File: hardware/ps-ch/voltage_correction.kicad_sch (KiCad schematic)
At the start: 35 parts, among them Q10 MMBT3904, Q5 MMBT3906, Q6 MMBT3906, Q7 MMBT3904, Q8 MMBT3904, U7 OPA992IDCKR, U8 OPA992IDCKR

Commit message: did some wiring
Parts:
- removed R37: R, symbol Device:R
- added C39, C42, C43, C75: C, symbol Device:C
- added L12: L, symbol Device:L
- added R29, R30, R31, R32, R33, R34: R, symbol Device:R
- added U9: OPA992IDCKR, symbol ps-ch:OPA992IDCKR
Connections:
- net GND: now also C42.2, C43.2, C75.2, R32.2, R33.1, U9.2 (V-)
- net VDC: now also C75.1, L12.1
- net VSENSE_SCALED renamed VSENSE
- net VSENSE: now also C39.1, R29.1, U9.4
- new net: R31.2, R32.1, U9.1 (+)
- new net: C39.2, R29.2, R30.2, U9.3 (-)
- new net: C42.1, C43.1, L12.2, U9.5 (V+)
- new net VREF+: R34.2
- new net VSENSE+: R31.1, R34.1
- new net VSENSE-: R30.1, R33.2
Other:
- note added: "VOLTAGE CORRECTION"
- moved on the sheet: C32, C35, C37, C38, C40, C44, C45, C69, C70, L10, L11, Q10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

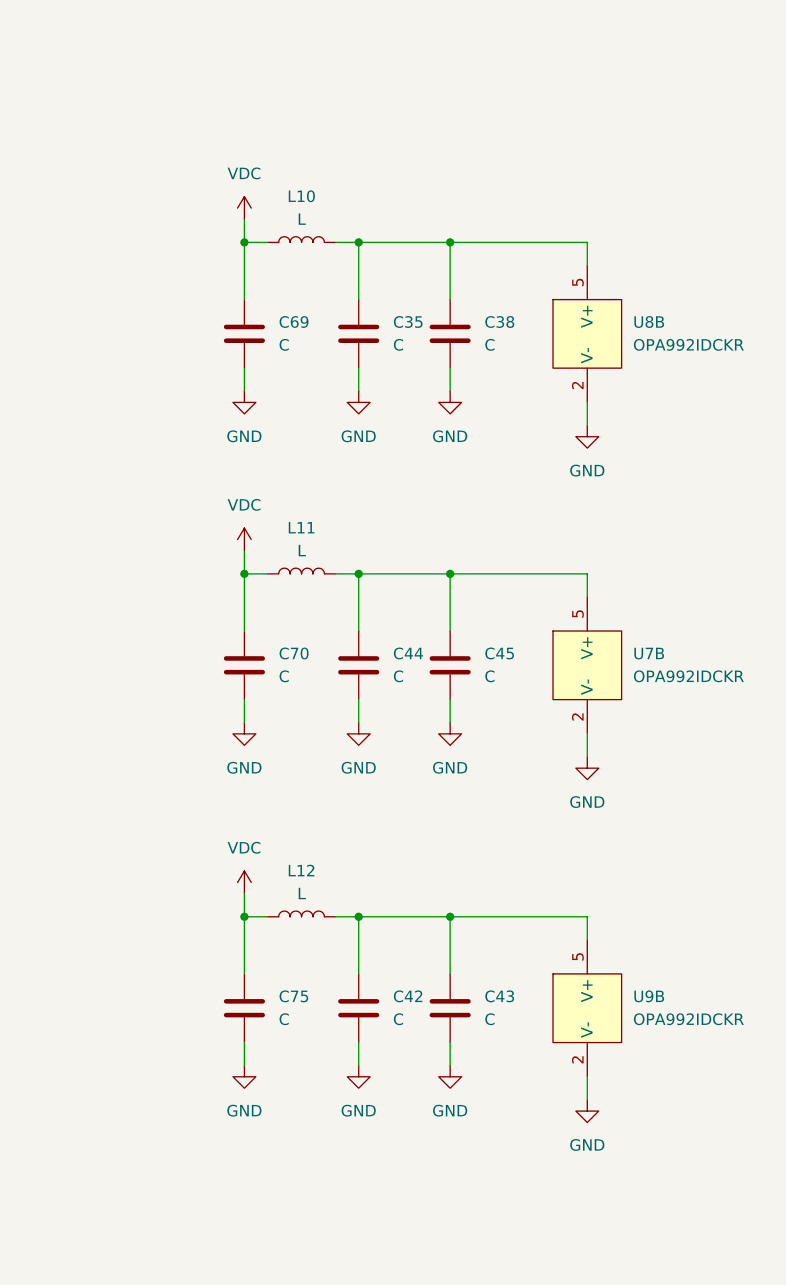
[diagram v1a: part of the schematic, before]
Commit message: added calculations and component values
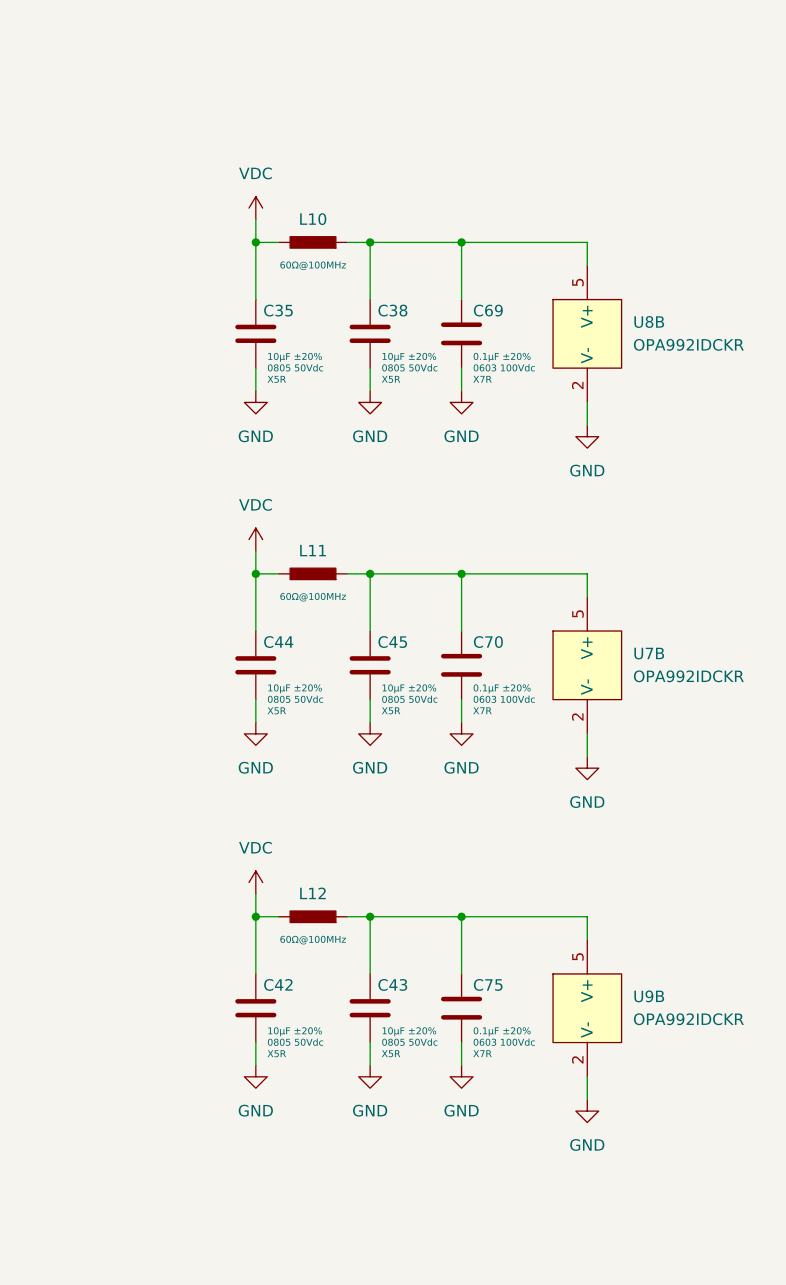
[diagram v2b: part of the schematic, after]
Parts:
- removed C35, C38, C42, C43, C44, C45, C69, C70, C75: C, symbol Device:C
- removed L10, L11, L12: L, symbol Device:L
- added C35, C38, C42, C43, C44, C45: 10μF 0805 50Vdc X5R ±20%, Capacitor_SMD:C_0805_2012Metric, symbol ps-ch:10μF 0805 50Vdc X5R ±20%
- added C69, C70, C75: 0.1μF 0603 100Vdc X7R ±20%, Capacitor_SMD:C_0603_1608Metric, symbol ps-ch:0.1μF 0603 100Vdc X7R ±20%
- added L10, L11, L12: 60Ω@100MHz, Inductor_SMD:L_0603_1608Metric, symbol ps-ch:74437349015
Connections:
- net GND: now also C35.1, C38.1, C42.1, C43.1, C44.1, C45.1, C69.1, C70.1, C75.1
- net VDC: now also C35.2, C42.2, C44.2, L10.2, L11.2, L12.2
- net at U8.5 (V+): now also C38.2, C69.2, L10.1
- net at U9.5 (V+): now also C43.2, C75.2, L12.1
- net at U7.5 (V+): now also C45.2, C70.2, L11.1

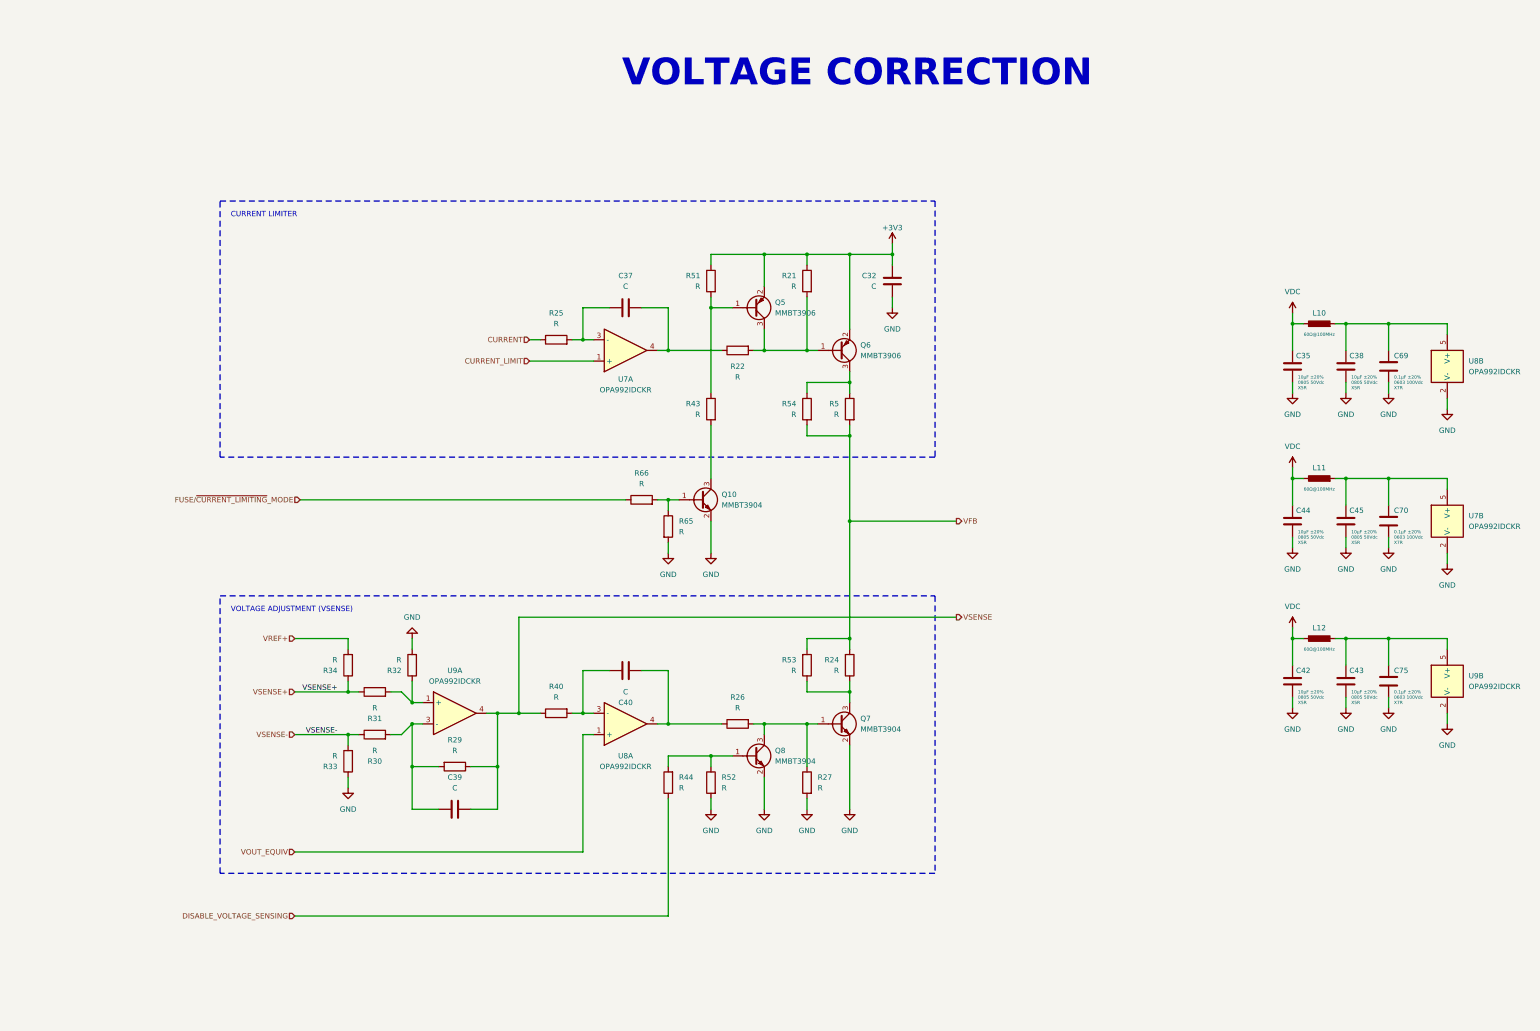
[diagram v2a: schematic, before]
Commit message: calculated voltage correction
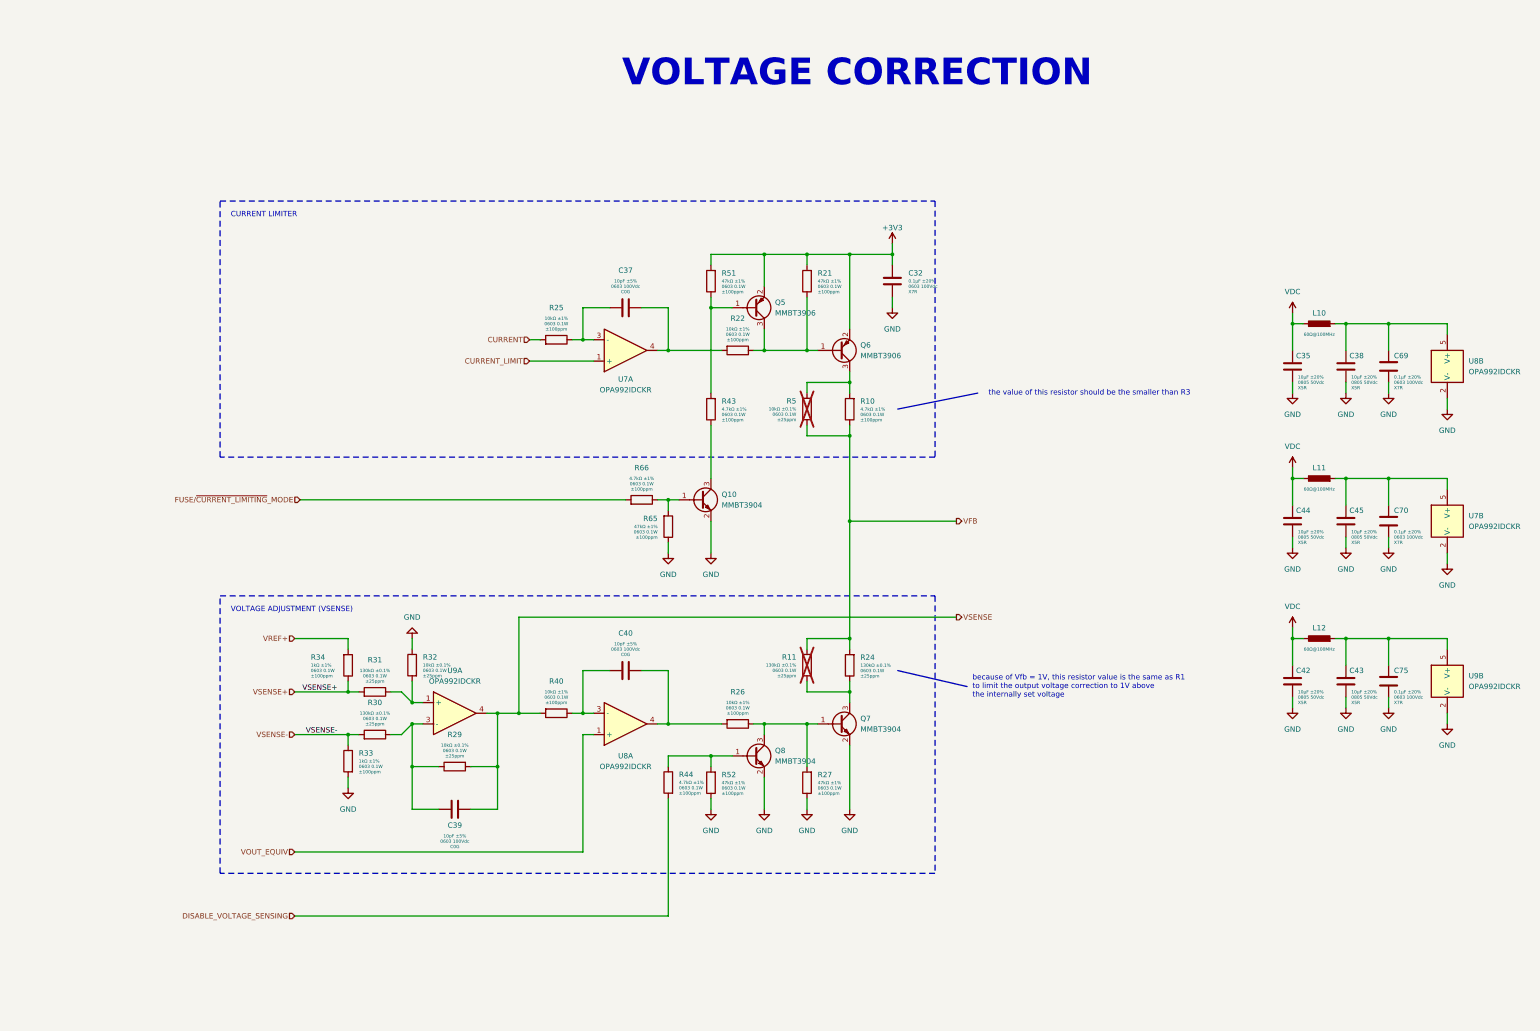
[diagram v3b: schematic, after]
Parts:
- removed R5, R53, R54: R, symbol Device:R
- added R10: 4.7kΩ 0603 0.1W ±1% ±100ppm/°C, Resistor_SMD:R_0603_1608Metric, symbol ps-ch:4.7kΩ 0603 0.1W ±1% ±100ppm/°C
- added R11: 130kΩ 0603 0.1W ±0.1% ±25ppm/°C, Resistor_SMD:R_0603_1608Metric, symbol ps-ch:130kΩ 0603 0.1W ±0.1% ±25ppm/°C
- added R5: 10kΩ 0603 0.1W ±0.1% ±25ppm/°C, Resistor_SMD:R_0603_1608Metric, symbol ps-ch:10kΩ 0603 0.1W ±0.1% ±25ppm/°C
- C32: value C -> 0.1μF 0603 100Vdc X7R ±20%; footprint (none) -> Capacitor_SMD:C_0603_1608Metric; symbol Device:C -> ps-ch:0.1μF 0603 100Vdc X7R ±20%; DisplayValue0 (none) -> 0.1μF ±20%; DisplayValue1 (none) -> 0603 100Vdc; DisplayValue2 (none) -> X7R; Manufacturer (none) -> Murata; Manufacturer Part Number (none) -> GRM188R72A104MA35
- C37, C39, C40: value C -> 10pF 0603 100Vdc C0G ±5%; footprint (none) -> Capacitor_SMD:C_0603_1608Metric; symbol Device:C -> ps-ch:10pF 0603 100Vdc C0G ±5%; DisplayValue0 (none) -> 10pF ±5%; DisplayValue1 (none) -> 0603 100Vdc; DisplayValue2 (none) -> C0G; Manufacturer (none) -> Murata; Manufacturer Part Number (none) -> GCM1885C2A100JA16
- R21, R27, R51, R52, R65: value R -> 47kΩ 0603 0.1W ±1% ±100ppm/°C; footprint (none) -> Resistor_SMD:R_0603_1608Metric; symbol Device:R -> ps-ch:47kΩ 0603 0.1W ±1% ±100ppm/°C; DisplayValue0 (none) -> 47kΩ ±1%; DisplayValue1 (none) -> 0603 0.1W; DisplayValue2 (none) -> ±100ppm; Manufacturer (none) -> Yageo; Manufacturer Part Number (none) -> AC0603FR-0747L
- R22, R25, R26, R40: value R -> 10kΩ 0603 0.1W ±1% ±100ppm/°C; footprint (none) -> Resistor_SMD:R_0603_1608Metric; symbol Device:R -> ps-ch:10kΩ 0603 0.1W ±1% ±100ppm/°C; DisplayValue0 (none) -> 10kΩ ±1%; DisplayValue1 (none) -> 0603 0.1W; DisplayValue2 (none) -> ±100ppm; Manufacturer (none) -> Yageo; Manufacturer Part Number (none) -> AC0603FR-0710KL
- R24, R30, R31: value R -> 130kΩ 0603 0.1W ±0.1% ±25ppm/°C; footprint (none) -> Resistor_SMD:R_0603_1608Metric; symbol Device:R -> ps-ch:130kΩ 0603 0.1W ±0.1% ±25ppm/°C; DisplayValue0 (none) -> 130kΩ ±0.1%; DisplayValue1 (none) -> 0603 0.1W; DisplayValue2 (none) -> ±25ppm; Manufacturer (none) -> Yageo; Manufacturer Part Number (none) -> RT0603BRD07130KL
- R29, R32: value R -> 10kΩ 0603 0.1W ±0.1% ±25ppm/°C; footprint (none) -> Resistor_SMD:R_0603_1608Metric; symbol Device:R -> ps-ch:10kΩ 0603 0.1W ±0.1% ±25ppm/°C; DisplayValue0 (none) -> 10kΩ ±0.1%; DisplayValue1 (none) -> 0603 0.1W; DisplayValue2 (none) -> ±25ppm; Manufacturer (none) -> Yageo; Manufacturer Part Number (none) -> RT0603BRD0710KL
- R33, R34: value R -> 1kΩ 0603 0.1W ±1% ±100ppm/°C; footprint (none) -> Resistor_SMD:R_0603_1608Metric; symbol Device:R -> ps-ch:1kΩ 0603 0.1W ±1% ±100ppm/°C; DisplayValue0 (none) -> 1kΩ ±1%; DisplayValue1 (none) -> 0603 0.1W; DisplayValue2 (none) -> ±100ppm; Manufacturer (none) -> Yageo; Manufacturer Part Number (none) -> AC0603FR-071KL
- R43, R44, R66: value R -> 4.7kΩ 0603 0.1W ±1% ±100ppm/°C; footprint (none) -> Resistor_SMD:R_0603_1608Metric; symbol Device:R -> ps-ch:4.7kΩ 0603 0.1W ±1% ±100ppm/°C; DisplayValue0 (none) -> 4.7kΩ ±1%; DisplayValue1 (none) -> 0603 0.1W; DisplayValue2 (none) -> ±100ppm; Manufacturer (none) -> Yageo; Manufacturer Part Number (none) -> AC0603FR-074k7L
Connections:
- net +3V3: now also C32.2, R21.2, R51.2; no longer C32.1, R21.1, R51.1
- net CURRENT: now also R25.2; no longer R25.1
- net DISABLE_VOLTAGE_SENSING: now also R44.2; no longer R44.1
- net FUSE/~{CURRENT_LIMITING}_MODE: now also R66.2; no longer R66.1
- net GND: now also C32.1, R27.1, R32.1, R33.2, R52.1, R65.1; no longer C32.2, R27.2, R32.2, R33.1, R52.2, R65.2
- net VFB: now also R10.1, R11.1, R5.2
- net VSENSE: now also R29.2, R40.2; no longer R29.1, R40.1
- net VSENSE+: now also R31.2; no longer R31.1
- net VSENSE-: now also R30.2, R33.1; no longer R30.1, R33.2
- net at Q7.1 (B), Q8.3 (C): now also R26.1, R27.2; no longer R26.2, R27.1
- net at Q7.3 (C), R24.1: now also R11.2
- net at Q5.3 (C), Q6.1 (B): now also R21.1, R22.1; no longer R21.2, R22.2
- net at Q6.3 (C): now also R10.2, R5.1
- net at C39.2, U9.3 (-): now also R29.1, R30.1; no longer R29.2, R30.2
- net at Q10.3 (C): now also R43.1; no longer R43.2
- new net: R31.1, R32.2, U9.1 (+)
- new net: Q8.1 (B), R44.1, R52.2
- new net: Q10.1 (B), R65.2, R66.1
- new net: C40.1, R40.1, U8.3 (-)
- new net: C40.2, R26.2, U8.4
- new net: Q5.1 (B), R43.2, R51.1
- new net: C37.1, R22.2, U7.4
- new net: C37.2, R25.1, U7.3 (-)
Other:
- note added: "because of Vfb = 1V, this resistor value is the same as R1 to limit the output voltage correction to 1V above the internally set voltage"
- note added: "the value of this resistor should be the smaller than R3"
- moved on the sheet: C39, R34

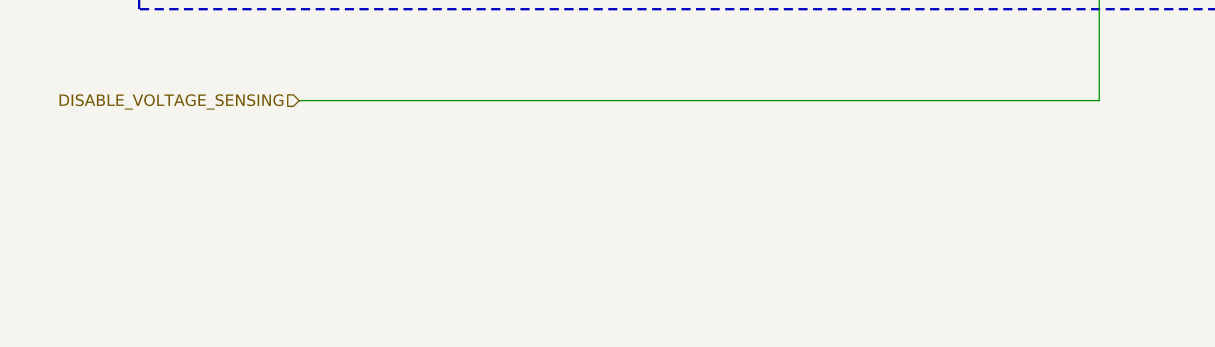
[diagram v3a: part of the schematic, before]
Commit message: wired adc/added resolutions
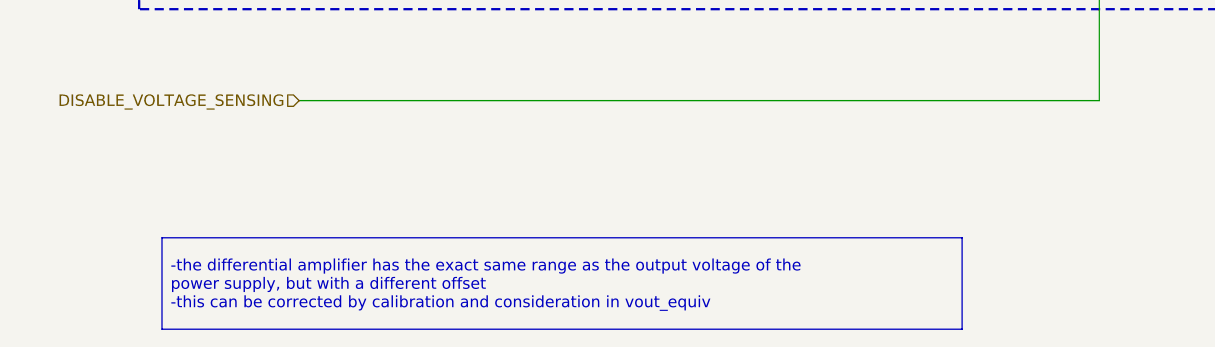
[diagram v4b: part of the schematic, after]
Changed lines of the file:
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@@
+		)
+	)
+	(text_box "-the differential amplifier has the exact same range as the output voltage of the power supply, but with a different offset\n-this can be corrected by calibration and consideration in vout_equiv"
+		(exclude_from_sim no)
+		(at 63.5 254 0)
+		(size 88.9 10.16)
+		(margins 0.9525 0.9525 0.9525 0.9525)
+		(stroke
+			(width 0)
+			(type solid)
+		)
+		(fill
+			(type none)
+		)
+		(effects
+			(font
+				(size 1.27 1.27)
+			)
+			(justify left)
 		)
 	)
